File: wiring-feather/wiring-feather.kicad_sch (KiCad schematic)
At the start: 27 parts, among them J1 M Battery 1, J10 GND_TEST, J11 I2C_TEST, J12 3V3, J13 GND_TEST, J14 BATT2-Charge, J16 BATT1-Charge, J2 M Battery 1, J3 Screw_Terminal_01x02, J4 Screw_Terminal_01x02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

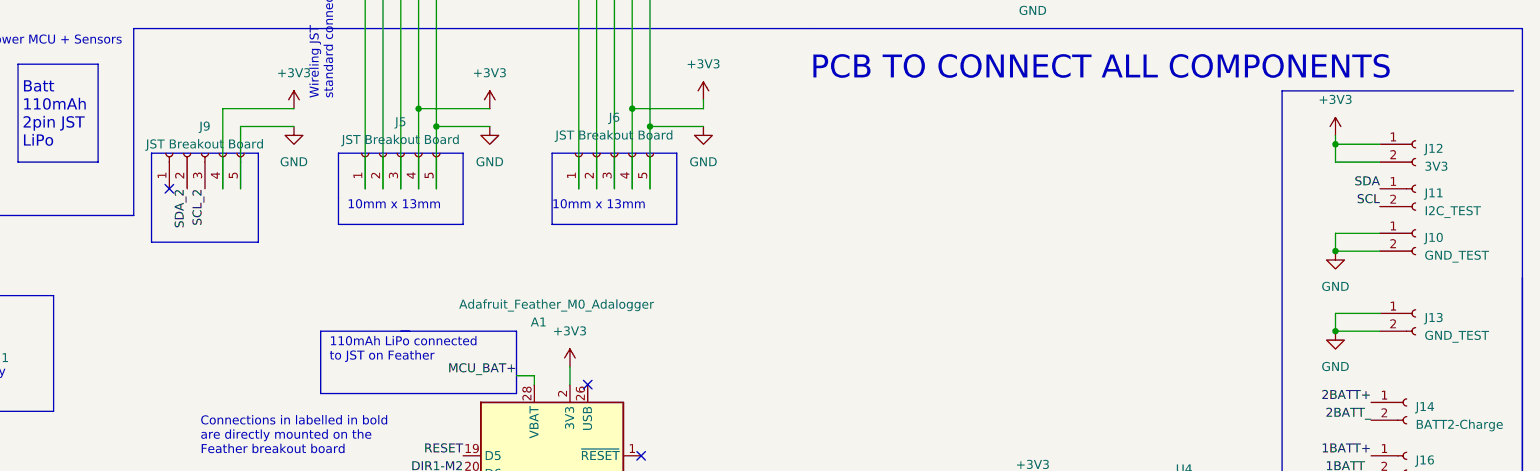
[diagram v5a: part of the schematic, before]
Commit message: design checks and silkscreen done
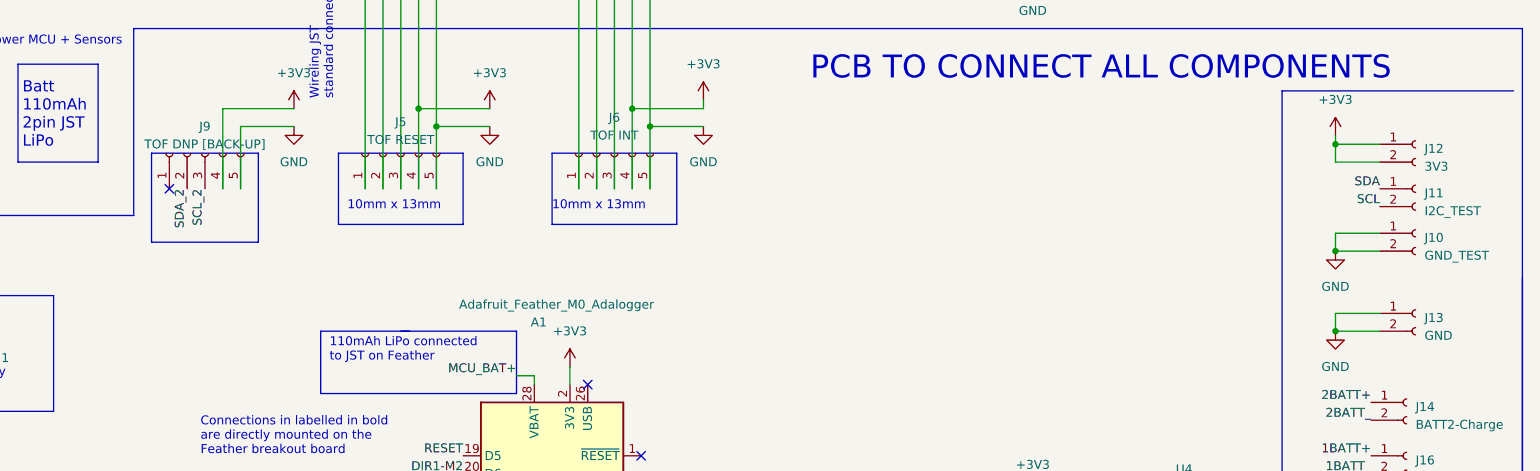
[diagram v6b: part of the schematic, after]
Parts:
- J13: value GND_TEST -> GND
- J3: value Screw_Terminal_01x02 -> PWR M1
- J5: value JST Breakout Board -> TOF RESET
- J6: value JST Breakout Board -> TOF INT
- J7: value Screw_Terminal_01x02 -> ENC M2
- J8: value Screw_Terminal_01x02 -> ENC M1
- J9: value JST Breakout Board -> TOF DNP [BACK-UP]
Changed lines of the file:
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@@
       (effects (font (size 1.27 1.27)) (justify left))
     )
-    (property "Value" "Screw_Terminal_01x02" (at 176.5301 146.05 90)
+    (property "Value" "ENC M2" (at 176.5301 146.05 90)
       (effects (font (size 1.27 1.27)) (justify right) hide)
     )
@@
       (effects (font (size 1.27 1.27)) (justify left))
     )
-    (property "Value" "GND_TEST" (at 269.24 103.505 0)
+    (property "Value" "GND" (at 269.24 103.505 0)
       (effects (font (size 1.27 1.27)) (justify left))
     )
@@
       (effects (font (size 1.27 1.27)) (justify left))
     )
-    (property "Value" "Screw_Terminal_01x02" (at 176.5301 152.4 90)
+    (property "Value" "ENC M1" (at 176.5301 152.4 90)
       (effects (font (size 1.27 1.27)) (justify right) hide)
     )
@@
       (effects (font (size 1.27 1.27)))
     )
-    (property "Value" "JST Breakout Board" (at 95.25 76.2 90)
+    (property "Value" "TOF DNP [BACK-UP]" (at 95.25 76.2 90)
       (effects (font (size 1.27 1.27)))
     )
@@
       (effects (font (size 1.27 1.27)))
     )
-    (property "Value" "JST Breakout Board" (at 123.19 75.565 90)
+    (property "Value" "TOF RESET" (at 123.19 75.565 90)
       (effects (font (size 1.27 1.27)))
     )
@@
       (effects (font (size 1.27 1.27)))
     )
-    (property "Value" "JST Breakout Board" (at 153.67 74.93 90)
+    (property "Value" "TOF INT" (at 153.67 74.93 90)
       (effects (font (size 1.27 1.27)))
     )
@@
       (effects (font (size 1.27 1.27)) (justify left))
     )
-    (property "Value" "Screw_Terminal_01x02" (at 85.0901 144.78 90)
+    (property "Value" "PWR M1" (at 85.0901 144.78 90)
       (effects (font (size 1.27 1.27)) (justify right) hide)
     )
